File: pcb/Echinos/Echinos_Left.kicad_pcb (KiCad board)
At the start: 2 copper layers, 167.4 x 138.9 mm, 133 parts, among them J1 Conn_01x06_Socket, J2 Conn_01x06_Socket, J3 Conn_01x06_Socket, J5 Conn_01x05_Socket, J6 USB_B_Micro, J7 Conn_01x04_Socket, J8 USB_C_Receptacle_USB2.0, SW111 SW_Push, SW112 SW_Push, SW113 SW_Push, SW114 SW_Push, SW115 SW_Push, SW122 SW_Push, SW123 SW_Push, SW124 SW_Push, SW125 SW_Push, SW131 SW_Push, SW132 SW_Push, SW133 SW_Push, SW134 SW_Push, SW135 SW_Push, SW141 SW_Push, SW142 SW_Push, SW143 SW_Push, SW144 SW_Push, SW145 SW_Push, SW151 SW_Push, SW152 SW_Push, SW153 SW_Push, SW154 SW_Push, SW155 SW_Push, SW2 Boot, SW3 Reset, SW4 Reset, SW5 Boot, U2 USBLC6-2P6, U3 XC6210B332MR-G, U4 W25Q128JVP, U5 RP2040, U7 USBLC6-2P6, U8 74LVC1T45, Y2 Crystal_GND24

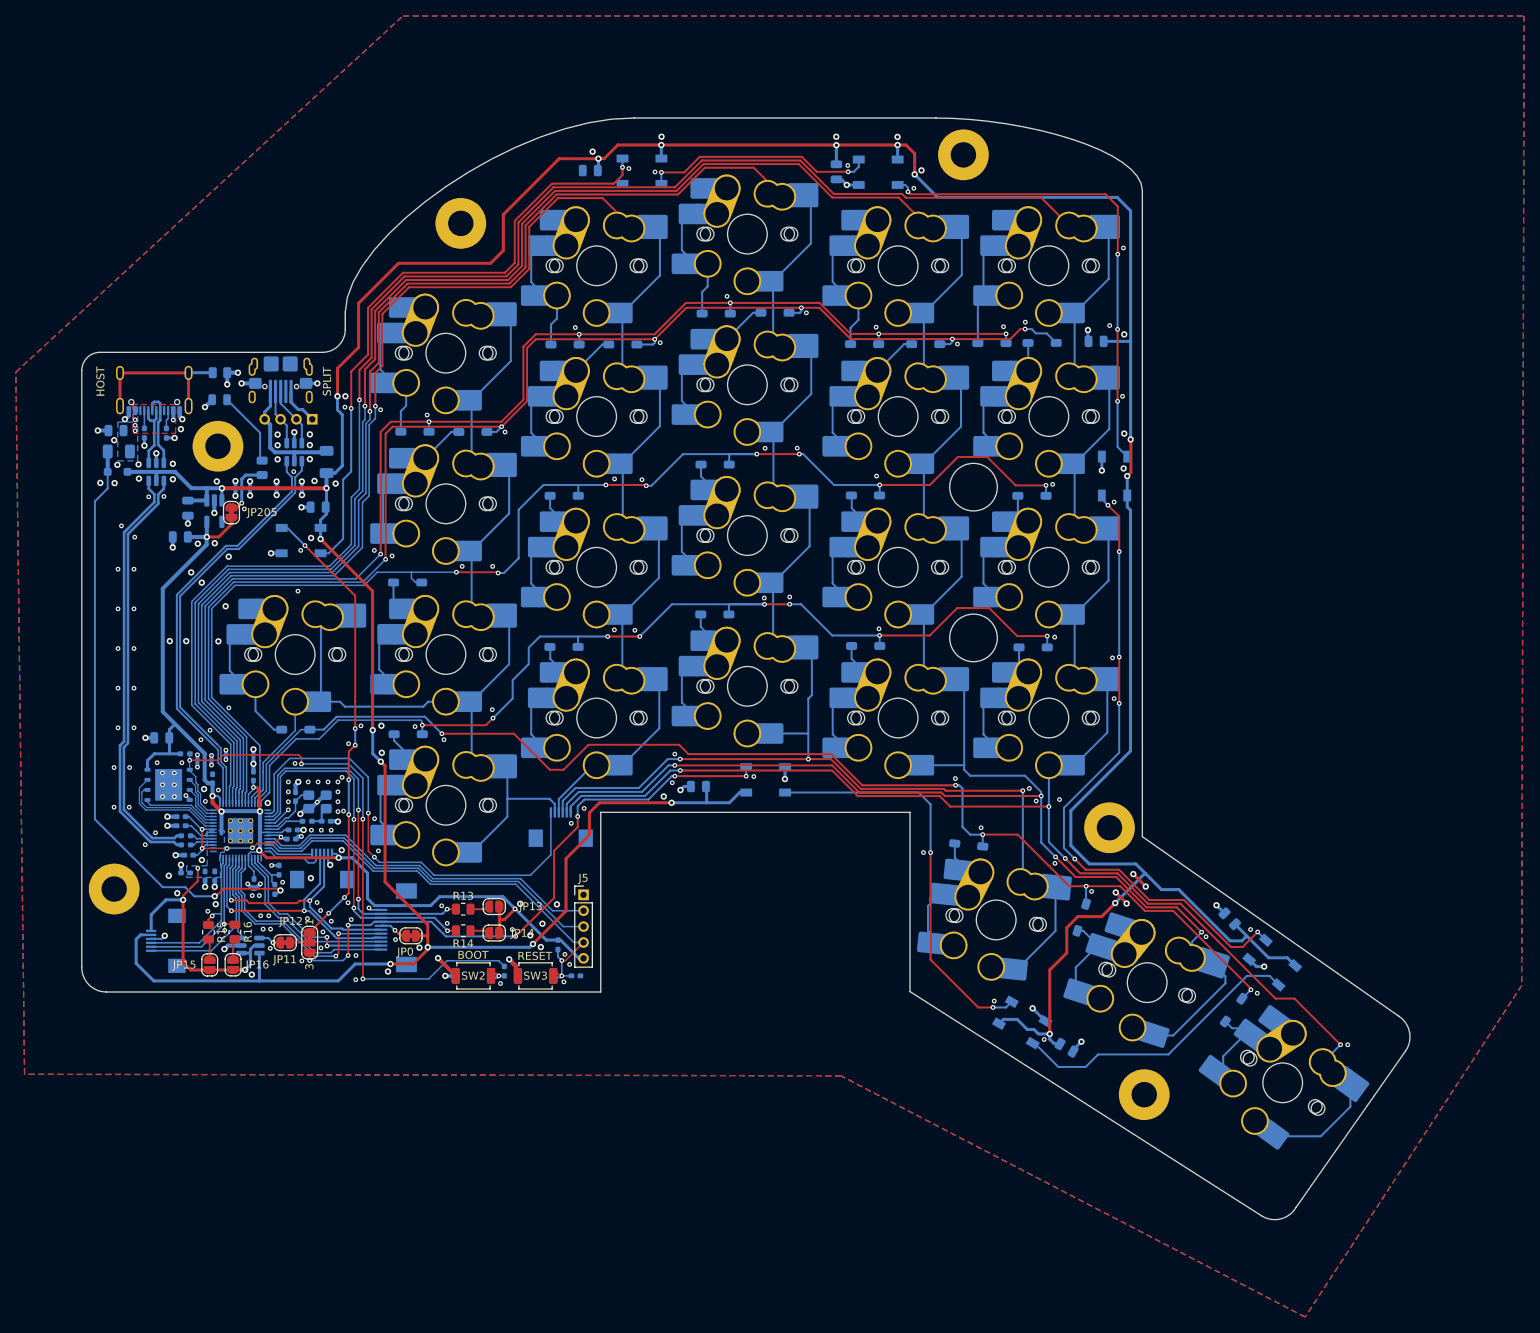
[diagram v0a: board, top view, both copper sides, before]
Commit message: [PCB] - Save last state with on board RP2040.   - Create right side and route all components   - Component still on the bottom side to be able to merge both side for manufacturing
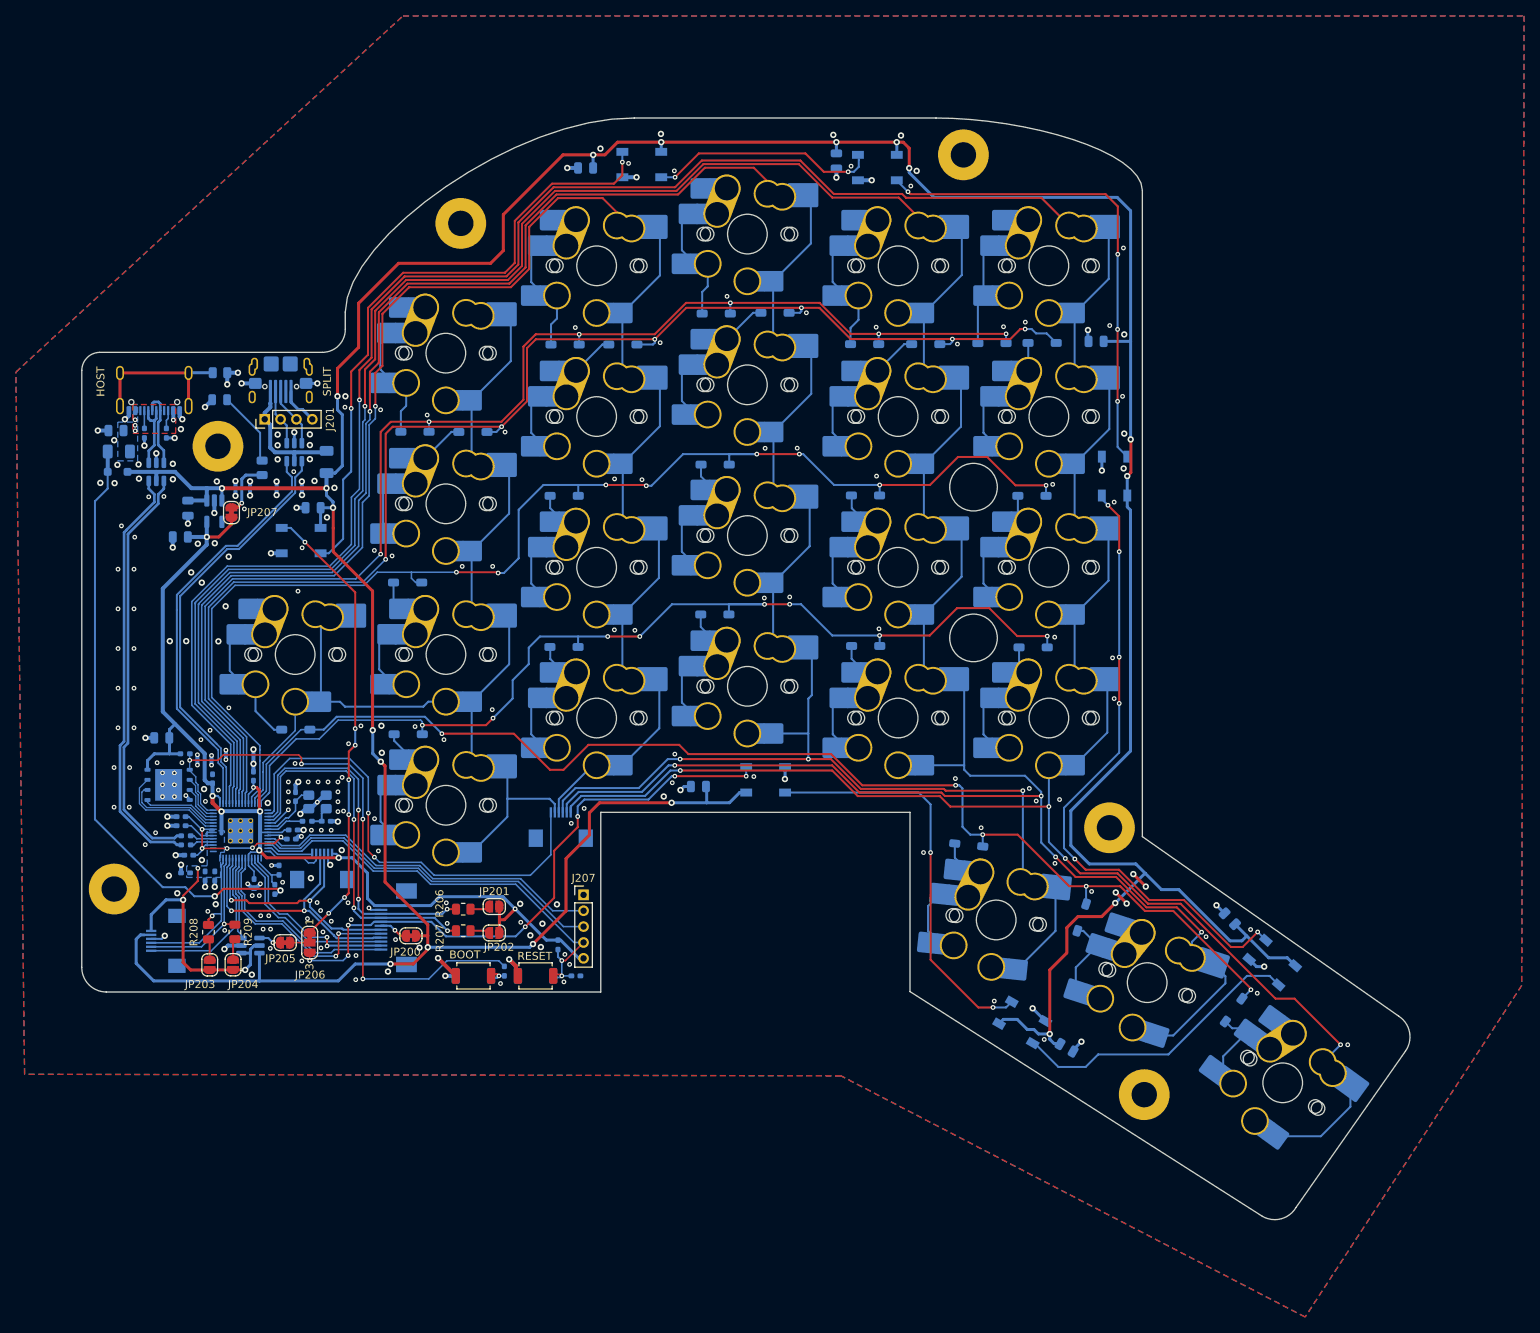
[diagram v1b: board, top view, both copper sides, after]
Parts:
- J201: renamed from J7; moved to F.Cu
- moved J201 6.00 mm to (69.2, 83.7)
- moved C217 1.38 mm to (141.2, 51.2)
- moved D225 0.84 mm to (116.7, 51.6)
- moved C216 0.68 mm to (109.6, 52.1)
- moved C215 0.64 mm to (75.3, 94.9)
- moved D226 0.60 mm to (146.4, 52.0)
- renumbered C6 to C200, C4 to C201, C5 to C202, C25 to C203, C7 to C204, C8 to C205, C9 to C206, C10 to C207, C18 to C208, C19 to C209, C20 to C210, C21 to C211, C22 to C212, C23 to C213, C24 to C214, C11 to C215, C12 to C216, C13 to C217, C14 to C218, C15 to C219, C16 to C220, C17 to C221, C3 to C222, C1 to C223, C2 to C224, D115 to D200, D114 to D201, D113 to D202, D112 to D203, D111 to D204, D125 to D205, D124 to D206, D123 to D207, D122 to D208, D135 to D209, D134 to D210, D133 to D211, D132 to D212, D131 to D213, D141 to D214, D145 to D215, D144 to D216, D143 to D217, D142 to D218, D155 to D219, D154 to D220, D153 to D221, D152 to D222, D151 to D223, D11 to D224, D12 to D225, D13 to D226, D14 to D227, D15 to D228, D16 to D229, D17 to D230, D3 to D231, D1 to D232, F2 to F200, F3 to F201, FB1 to FB200, H1 to H200, H2 to H201, H5 to H202, H3 to H203, H4 to H204, H6 to H205, J6 to J200, J4 to J202, J1 to J203, J2 to J204, J3 to J205, J8 to J206, J5 to J207, JP0 to JP200, JP13 to JP201, JP14 to JP202, JP15 to JP203, JP16 to JP204, JP11 to JP205, JP12 to JP206, JP205 to JP207, R5 to R200, R2 to R201, R4 to R202, R6 to R203, R10 to R204, R11 to R205, R13 to R206, R14 to R207, R15 to R208, R16 to R209, R7 to R210, R8 to R211, R9 to R212, R12 to R213, R1 to R214, SW115 to SW200, SW114 to SW201, SW113 to SW202, SW112 to SW203, SW111 to SW204, SW125 to SW205, SW124 to SW206, SW123 to SW207, SW122 to SW208, SW135 to SW209, SW134 to SW210, SW133 to SW211, SW132 to SW212, SW131 to SW213, SW145 to SW214, SW144 to SW215, SW143 to SW216, SW142 to SW217, SW141 to SW218, SW155 to SW219, SW154 to SW220, SW153 to SW221, SW152 to SW222, SW151 to SW223, SW2 to SW224, SW5 to SW225, SW4 to SW226, SW3 to SW227, U4 to U200, U5 to U201, U7 to U202, U8 to U203, U2 to U204, U3 to U205, Y2 to Y200
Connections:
- net /Backlight/backlight_in renamed /Split/Backlight/backlight_in
- net /P_USB+ renamed /Split/P_USB+
- net /P_USB- renamed /Split/P_USB-
- net /RP2040/GPIO12 renamed /Split/RP2040/GPIO12
- net /RP2040/GPIO18 renamed /Split/RP2040/GPIO18
- net /RP2040/GPIO19 renamed /Split/RP2040/GPIO19
- net /RP2040/QSPI_SCLK renamed /Split/RP2040/QSPI_SCLK
- net /RP2040/QSPI_SD0 renamed /Split/RP2040/QSPI_SD0
- net /RP2040/QSPI_SD1 renamed /Split/RP2040/QSPI_SD1
- net /RP2040/QSPI_SD2 renamed /Split/RP2040/QSPI_SD2
- net /RP2040/QSPI_SD3 renamed /Split/RP2040/QSPI_SD3
- net /RP2040/QSPI_SS renamed /Split/RP2040/QSPI_SS
- net /USB+ renamed /Split/USB+
- net /USB- renamed /Split/USB-
- J201 pad 1: GND -> VBUS_split
- J201 pad 2: P_RX -> P_TX
- J201 pad 3: P_TX -> P_RX
- J201 pad 4: VBUS_split -> GND
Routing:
- net GND: track 100.8 -> 103.6 mm, vias 273 -> 276
- net +5V: track 508.9 -> 511.5 mm
- net Net-(D224-DOUT): track 78.2 -> 79.0 mm
- net Net-(D225-DOUT): track 29.1 -> 28.3 mm

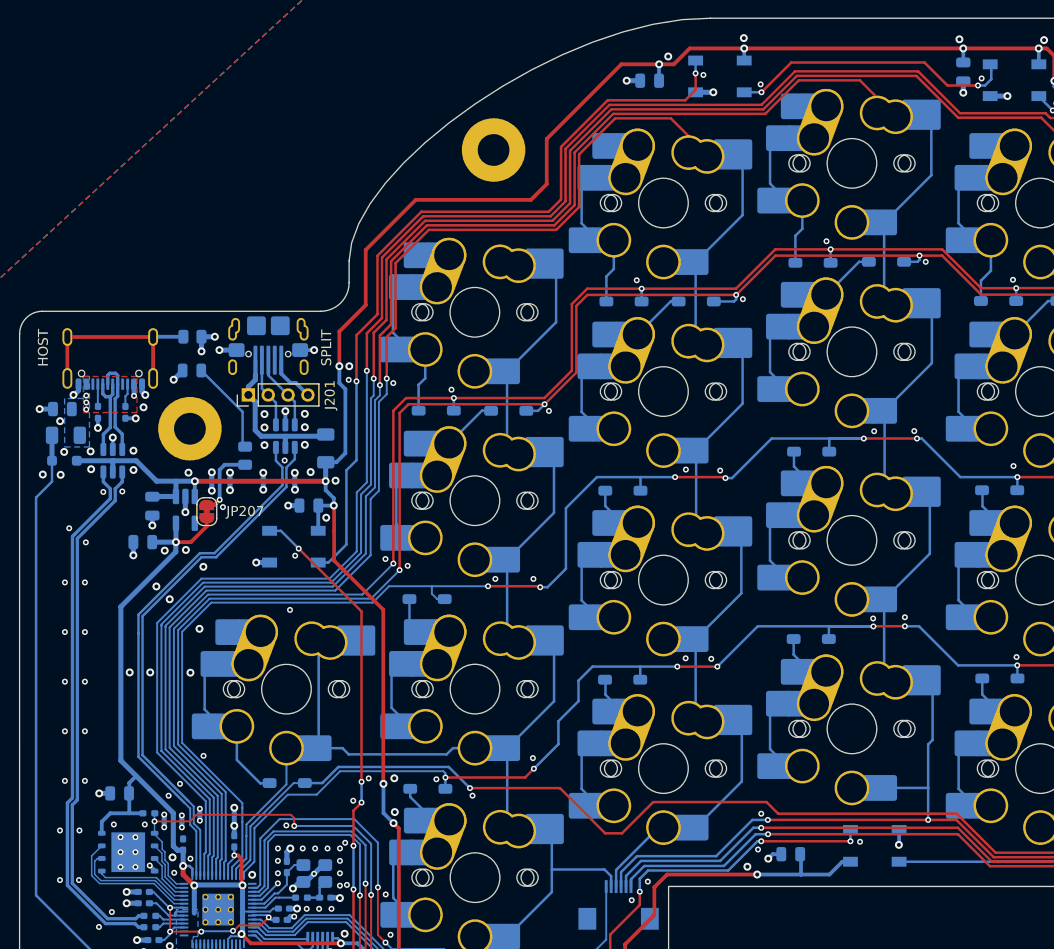
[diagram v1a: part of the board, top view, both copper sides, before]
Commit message: [PCB] - Save last state with on board RP2040.   - Fix flash component orientation for JLCPCB assembly   - Add logo + version   - Add TH in flash footprint and use the same zone fill method as for RP2040 footprint   - Improve ground planes under switches (right side)   - Move unused schematics to backup folder (will be used to create keyboard modules later)   - Add manufacturer and part name (mfr)   - Mark optional parts as DNP   - Resync with official RP2040 symbol and update pins matching
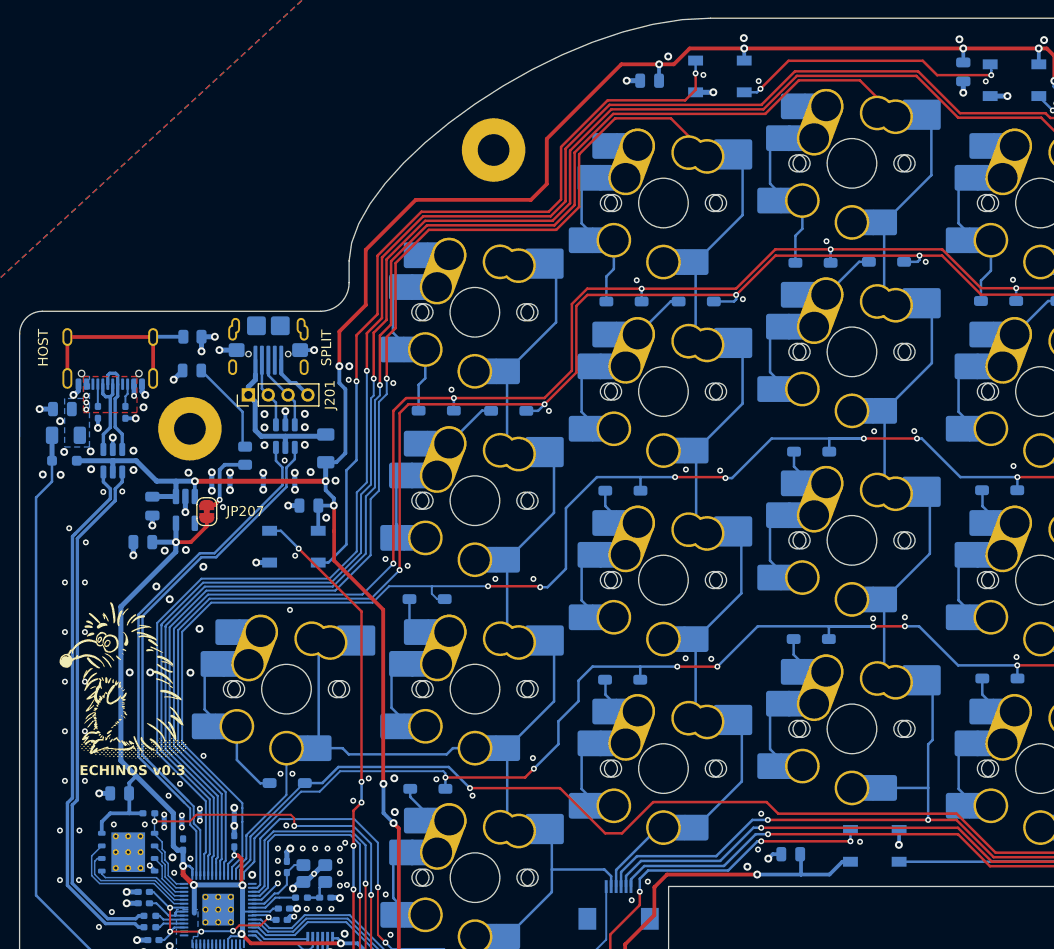
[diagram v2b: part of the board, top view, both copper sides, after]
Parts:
- added A1: Echinos Logo, Echinos:Graphics_Hedgehog, F.Cu at (56.5, 111.8)
- H200, H201, H202, H203, H204, H205: value MountHole -> M3
- J202: value ~ -> Conn_01x12_Socket
- U200: footprint Package_SON:WSON-8-1EP_6x5mm_P1.27mm_EP3.4x4mm -> Echinos:WSON-8-1EP_6x5mm_P1.27mm_EP3.4x4mm
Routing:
- net Net-(D225-DOUT): track 28.3 -> 27.3 mm
- net row2: track 130.5 -> 129.9 mm
- net row1: track 157.1 -> 156.5 mm
- net GND: vias 276 -> 272
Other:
- board text added: "ECHINOS v0.3"
